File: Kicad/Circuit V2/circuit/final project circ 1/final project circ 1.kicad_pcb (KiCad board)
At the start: 2 copper layers, 100.5 x 100 mm, 86 parts, among them J1 USB_B_Micro, J10 Conn_01x02_Female, J11 Conn_01x02_Female, J3 Conn_01x04_Female, J4 Conn_01x04_Female, J5 Conn_01x03_Female, J6 Conn_01x03_Female, J7 Conn_01x04_Female, J8 Conn_01x02_Female, J9 Conn_01x02_Female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

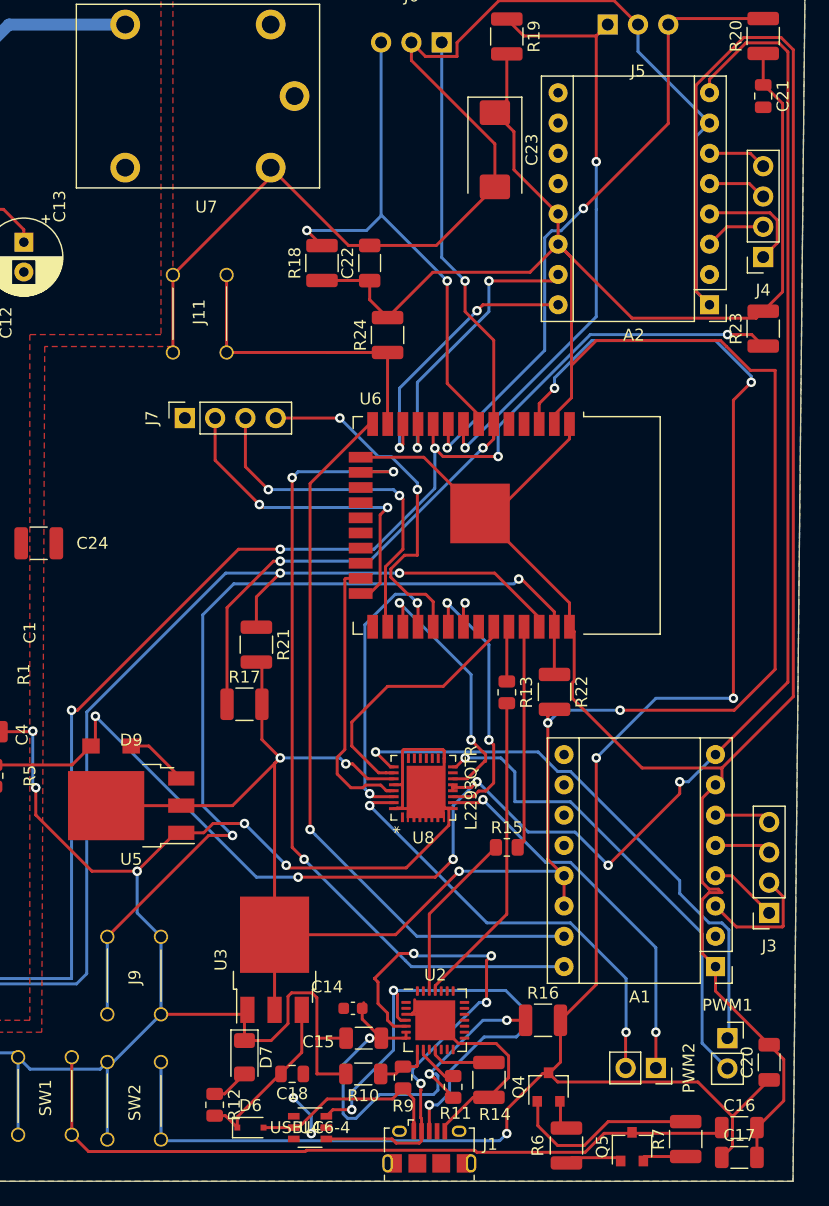
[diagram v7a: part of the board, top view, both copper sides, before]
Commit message: added 12 plug for power supplys
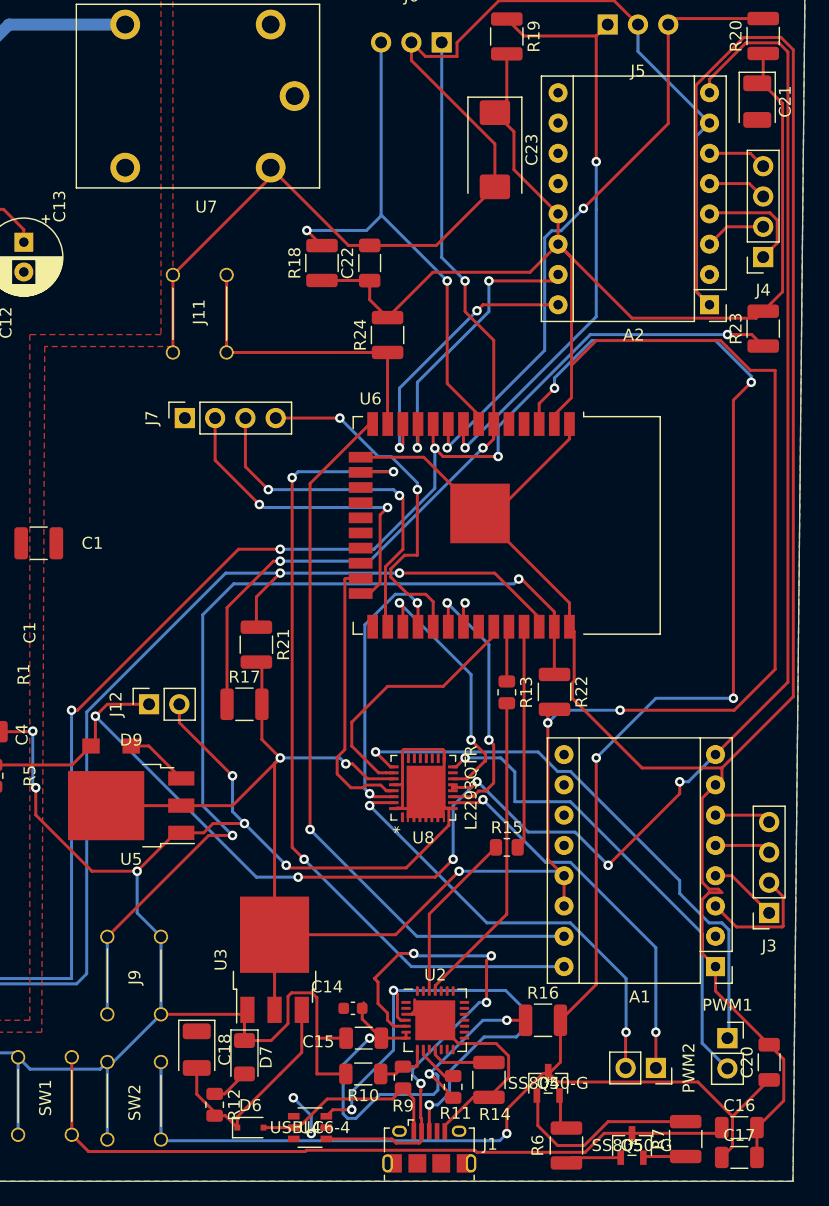
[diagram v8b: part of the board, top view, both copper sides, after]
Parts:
- added J12: Conn_01x02_Female, Connector_PinSocket_2.54mm:PinSocket_1x02_P2.54mm_Vertical, F.Cu at (357.0, 169.0)
- C18: footprint Capacitor_SMD:C_0805_2012Metric -> Capacitor_Tantalum_SMD:CP_EIA-3528-21_Kemet-B
- C21: value 22uF -> 22uF/10V; footprint Capacitor_SMD:C_0805_2012Metric -> Capacitor_Tantalum_SMD:CP_EIA-3528-21_Kemet-B
- Q4, Q5: footprint Package_TO_SOT_SMD:SC-59 -> bigboard:SS8050-G
- moved C18 8.26 mm to (361.0, 198.0), turned to 270 degrees
- moved C21 0.68 mm to (408.0, 118.5)
- moved Q4 0.32 mm to (390.5, 200.8), turned to 0 degrees
- moved Q5 0.10 mm to (397.5, 206.0), turned to 0 degrees
- renumbered C24 to C1
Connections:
- C1 pad 1: GND -> Net-(C1-Pad1)
- C10 pad 1: 12v -> GND1
- C10 pad 2: GND1 -> 12v
- C11 pad 1: Net-(C11-Pad2) -> GND1
- C11 pad 2: GND1 -> Net-(C11-Pad2)
- C12 pad 1: +VDC -> GND1
- C12 pad 2: GND1 -> +VDC
- C13 pad 1: Net-(C13-Pad2) -> GND1
- C13 pad 2: GND1 -> Net-(C13-Pad2)
- C8 pad 1: 12v -> GND1
- C8 pad 2: GND1 -> 12v
- C9 pad 1: 12v -> GND1
- C9 pad 2: GND1 -> 12v
- U7 pad 2: LINE -> +VDC
- U8 pad 2: GND -> Net-(U8-Pad2)
- U8 pad 3: GND -> Net-(U8-Pad3)
- U8 pad 33: GND -> (no net)
- U8 pad 4: GND -> Net-(U8-Pad4)
- U8 pad 5: GND -> Net-(U8-Pad5)
- U8 pad 6: GND -> Net-(U8-Pad6)
- U8 pad 7: GND -> Net-(U8-Pad7)
- U8 pad 8: GND -> Net-(U8-Pad8)
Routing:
- net GND: track 492.7 -> 504.9 mm, vias 7 -> 8
- net 12v: track 188.7 -> 193.6 mm
- net Net-(C18-Pad2): track 14.4 -> 19.0 mm
